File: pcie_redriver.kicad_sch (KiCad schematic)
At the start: 75 parts, among them U33 PI3EQX16904GL, U34 PI3EQX16904GL

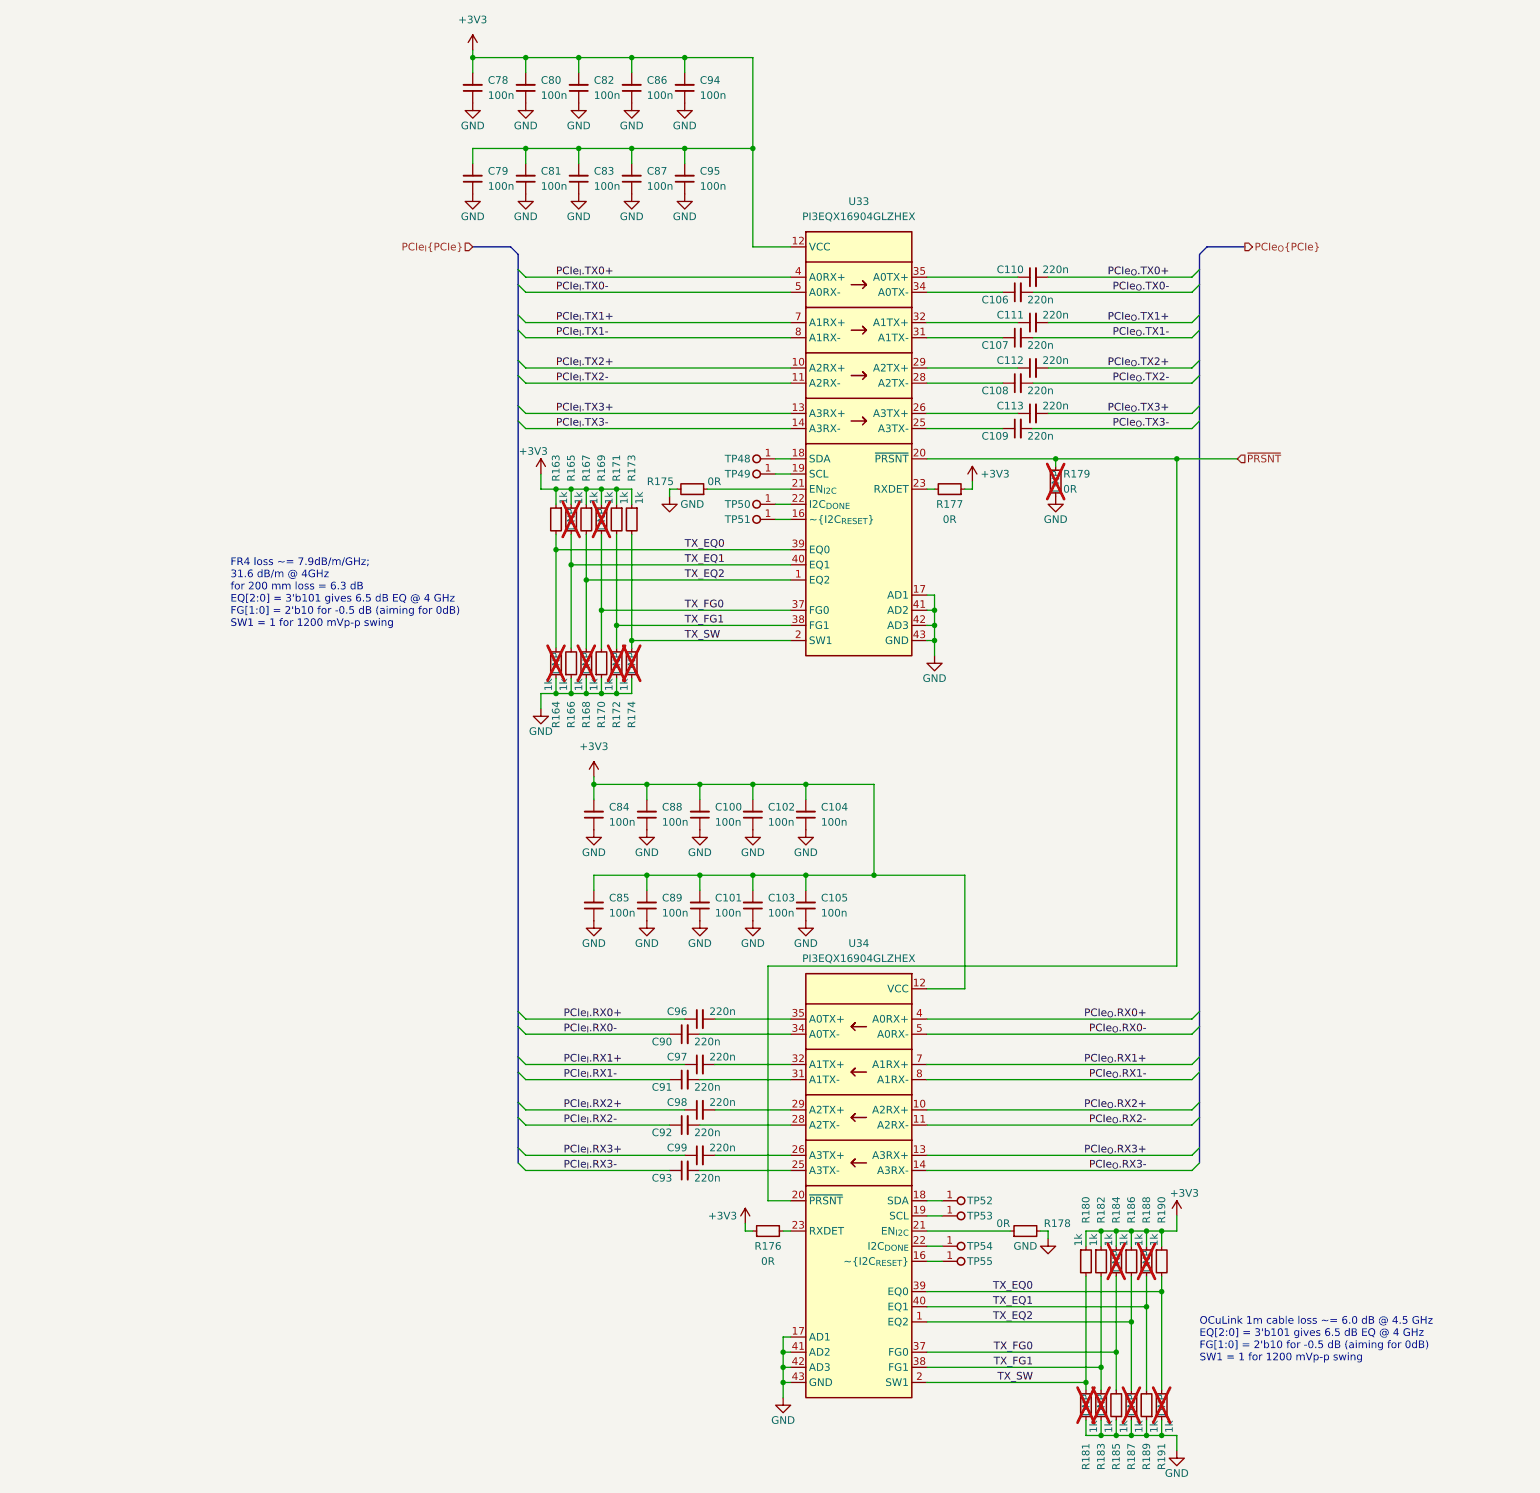
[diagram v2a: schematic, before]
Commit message: Reannotate schematic
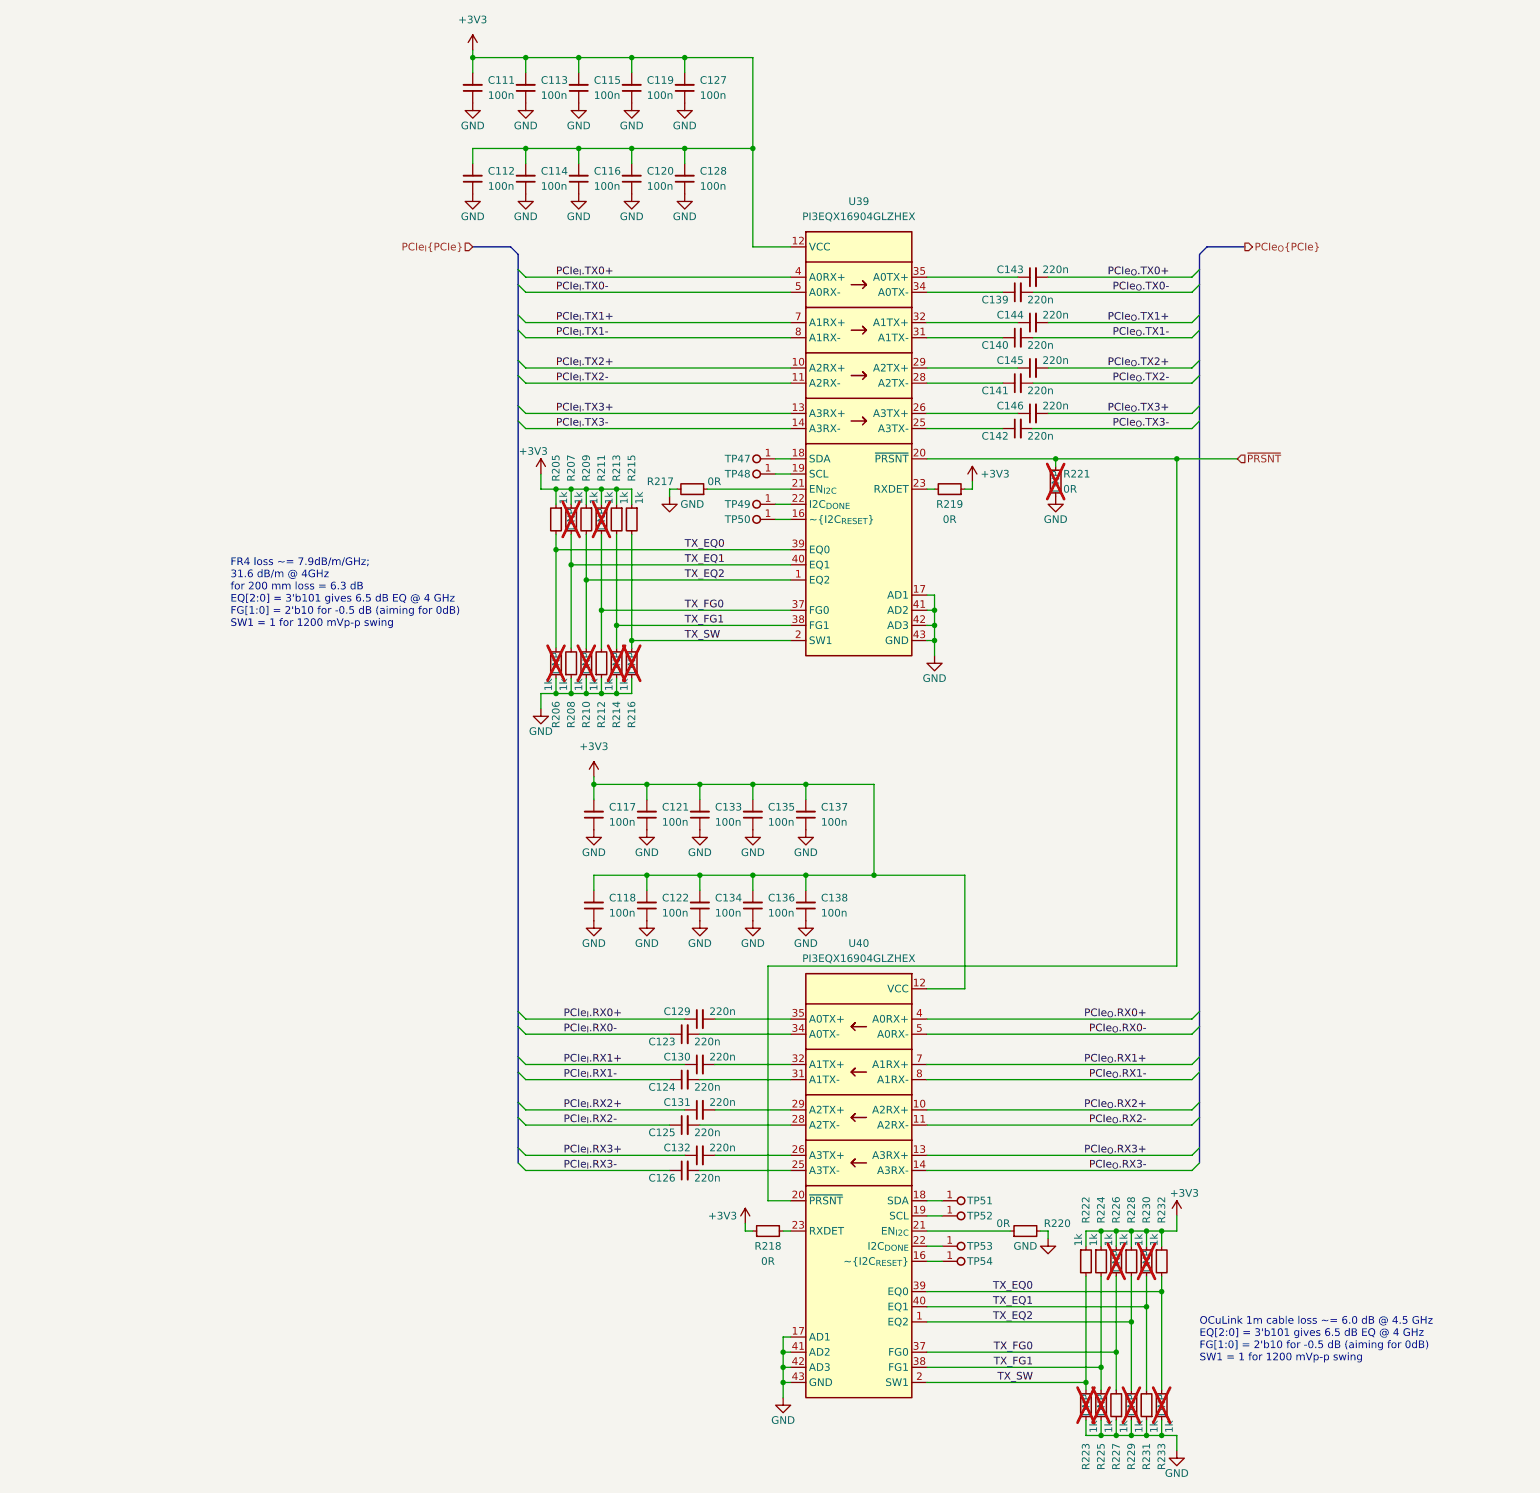
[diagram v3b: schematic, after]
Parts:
- renumbered C78 to C111, C79 to C112, C80 to C113, C81 to C114, C82 to C115, C83 to C116, C84 to C117, C85 to C118, C86 to C119, C87 to C120, C88 to C121, C89 to C122, C90 to C123, C91 to C124, C92 to C125, C93 to C126, C94 to C127, C95 to C128, C96 to C129, C97 to C130, C98 to C131, C99 to C132, C100 to C133, C101 to C134, C102 to C135, C103 to C136, C104 to C137, C105 to C138, C106 to C139, C107 to C140, C108 to C141, C109 to C142, C110 to C143, C111 to C144, C112 to C145, C113 to C146, R163 to R205, R164 to R206, R165 to R207, R166 to R208, R167 to R209, R168 to R210, R169 to R211, R170 to R212, R171 to R213, R172 to R214, R173 to R215, R174 to R216, R175 to R217, R176 to R218, R177 to R219, R178 to R220, R179 to R221, R180 to R222, R181 to R223, R182 to R224, R183 to R225, R184 to R226, R185 to R227, R186 to R228, R187 to R229, R188 to R230, R189 to R231, R190 to R232, R191 to R233, TP48 to TP47, TP49 to TP48, TP50 to TP49, TP51 to TP50, TP52 to TP51, TP53 to TP52, TP54 to TP53, TP55 to TP54, U33 to U39, U34 to U40

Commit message: Optimize BOM, reannotate
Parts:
- renumbered R205 to R202, R206 to R203, R207 to R204, R208 to R205, R209 to R206, R210 to R207, R211 to R208, R212 to R209, R213 to R210, R214 to R211, R215 to R212, R216 to R213, R217 to R214, R218 to R215, R219 to R216, R220 to R217, R221 to R218, R222 to R219, R223 to R220, R224 to R221, R225 to R222, R226 to R223, R227 to R224, R228 to R225, R229 to R226, R230 to R227, R231 to R228, R232 to R229, R233 to R230, TP47 to TP49, TP48 to TP50, TP49 to TP51, TP50 to TP52, TP51 to TP53, TP52 to TP54, TP53 to TP55, TP54 to TP56

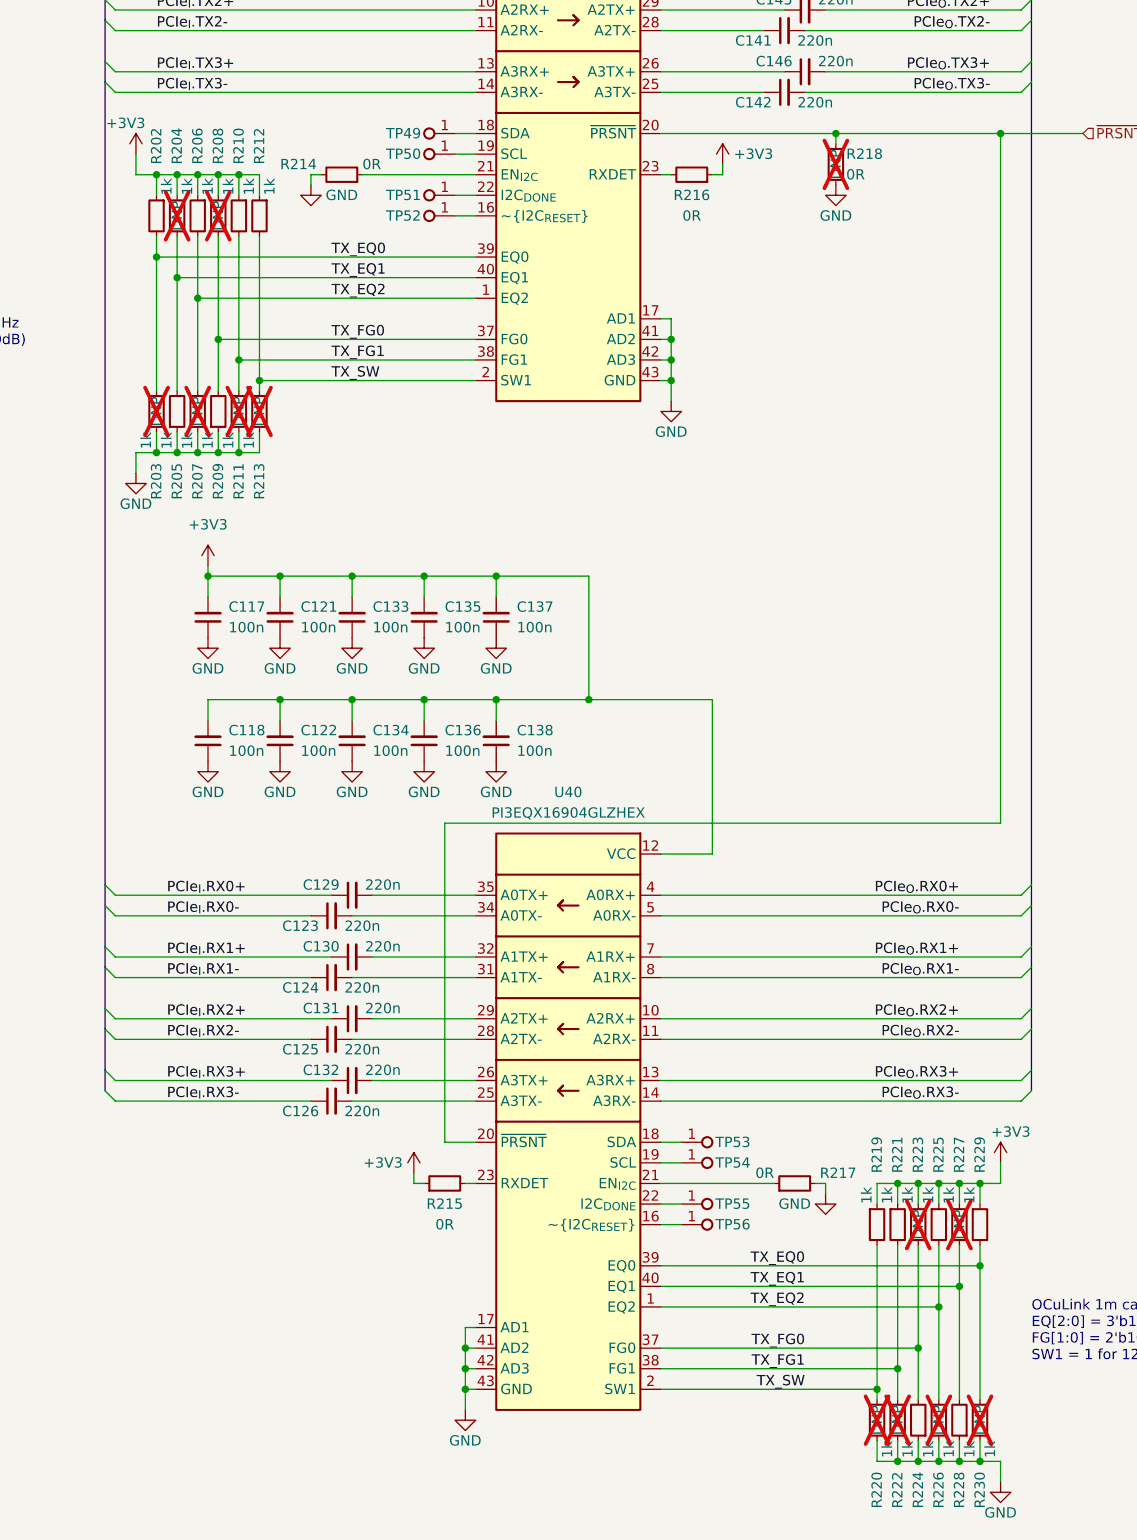
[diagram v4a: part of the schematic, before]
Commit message: Update components from the library
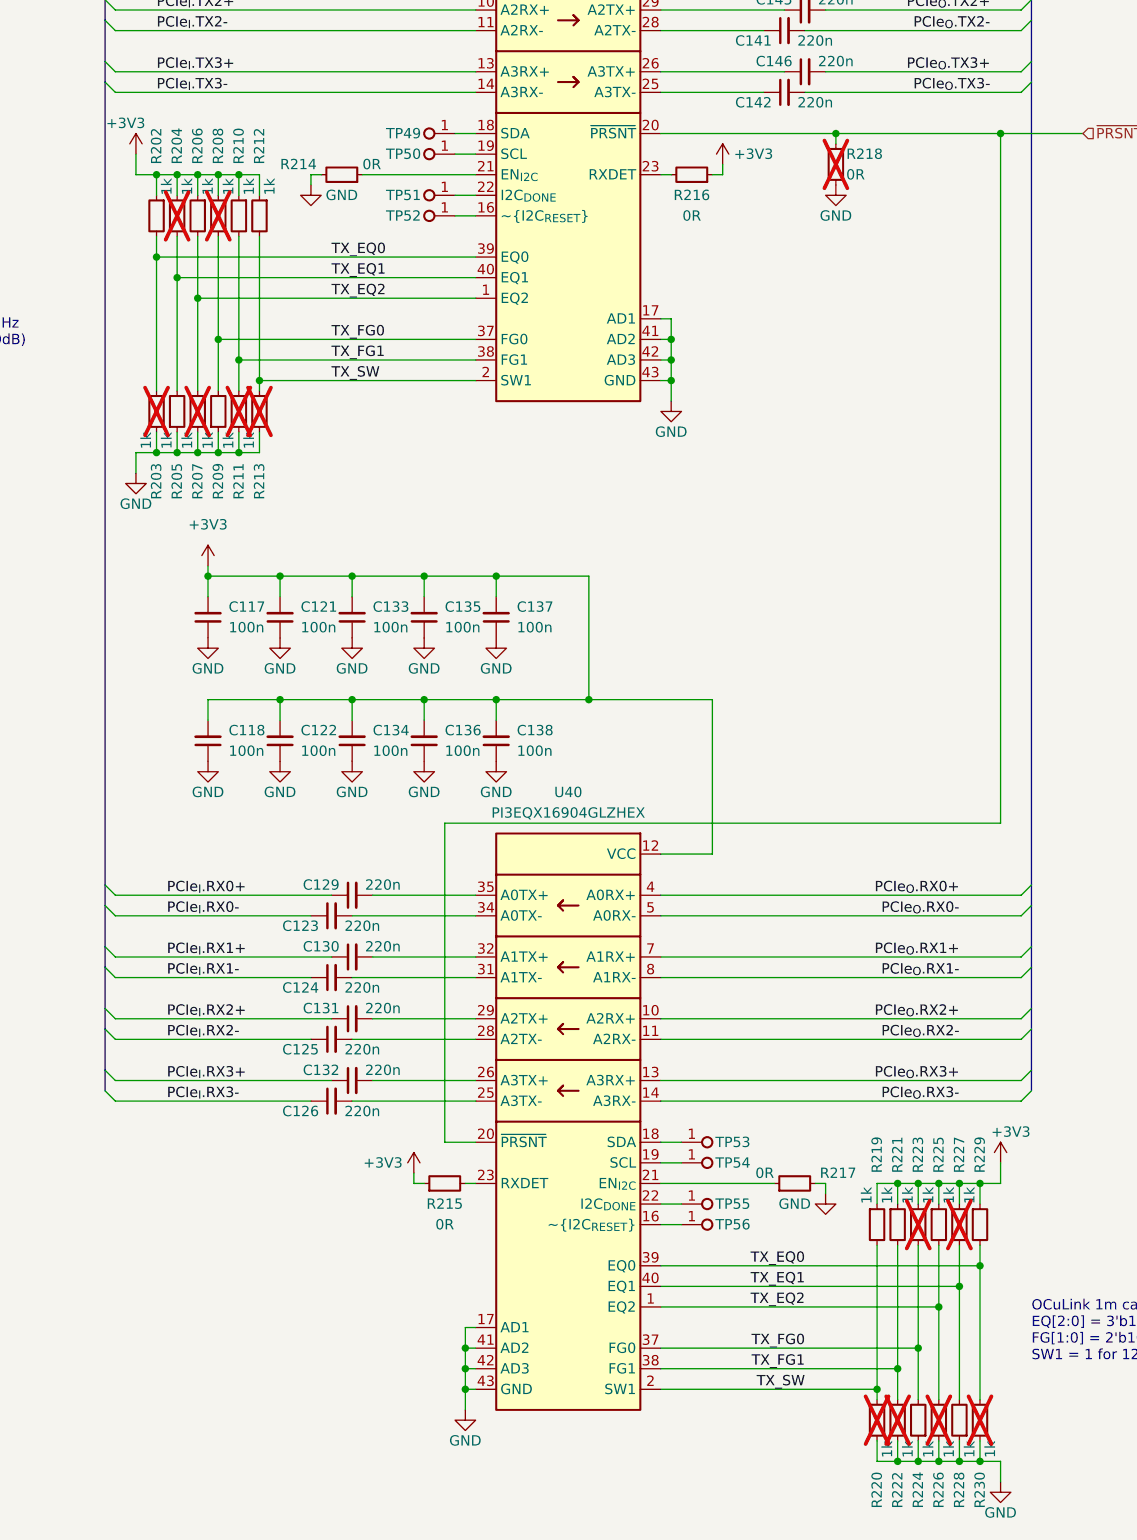
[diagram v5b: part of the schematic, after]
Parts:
- C111, C112, C113, C114, C115, C116, C117, C118, C119, C120, C121, C122, C123, C124, C125, C126, C127, C128, C129, C130, C131, C132, C133, C134, C135, C136, C137, C138, C139, C140, C141, C142, C143, C144, C145, C146, R202, R205, R206, R209, R210, R212, R214, R215, R216, R217, R219, R221, R224, R225, R228, R229, TP49, TP50, TP51, TP52, TP53, TP54, TP55, TP56: Public (none) -> False
- R203, R204, R207, R208, R211, R213, R218, R220, R222, R223, R226, R227, R230: DNP DNP -> (none); Public (none) -> False
